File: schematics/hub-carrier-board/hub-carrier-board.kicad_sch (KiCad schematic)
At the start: 15 parts, among them J2 PWR, SW101 MK-11C04-G013

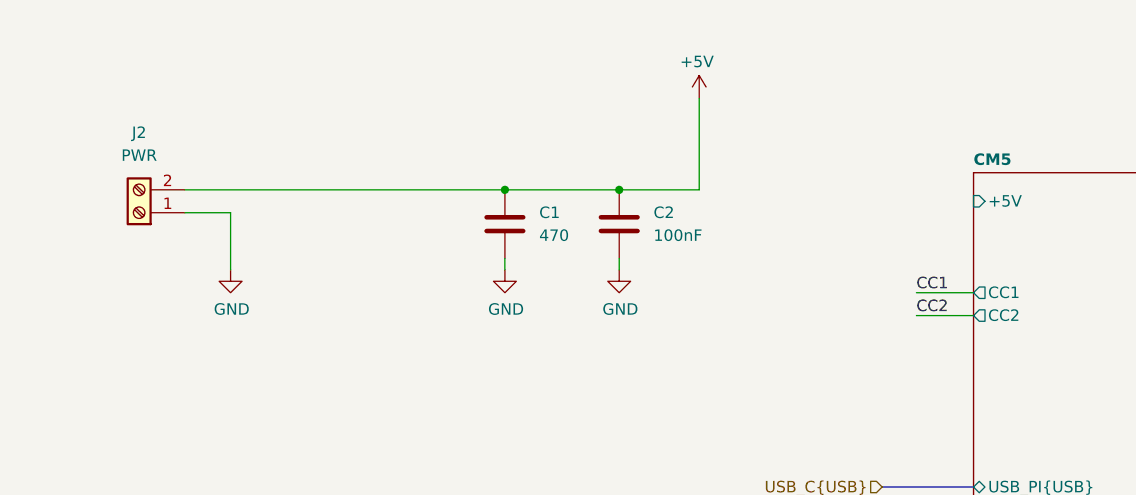
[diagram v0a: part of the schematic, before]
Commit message: chore(schematics): update hub carrier board and add project file
Updates CM5/USB sub-sheets and the top-level hub-carrier-board
schematic. Also tracks hub-carrier-board.kicad_pro, which had only
been committed on the feat/hub-carrier-board branch.

Co-Authored-By: Claude Opus 4.7 (1M context) <noreply@anthropic.com>
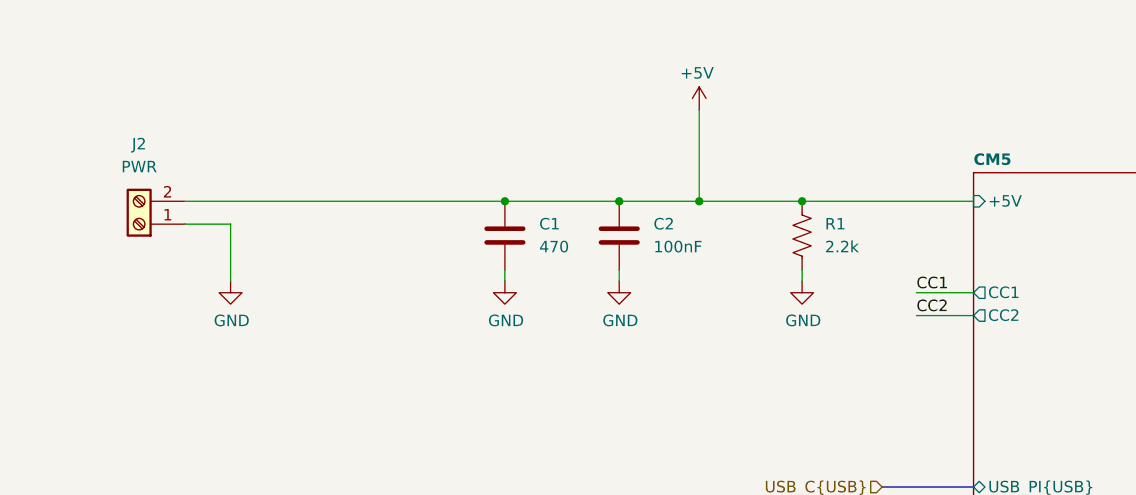
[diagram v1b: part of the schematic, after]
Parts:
- added R1: 2.2k, symbol Device:R_US
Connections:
- net +5V: now also R1.1
- net GND: now also R1.2
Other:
- moved on the sheet: C1, C2, J2
